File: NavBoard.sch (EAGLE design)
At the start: 11 parts, among them U2 LSM9DS1

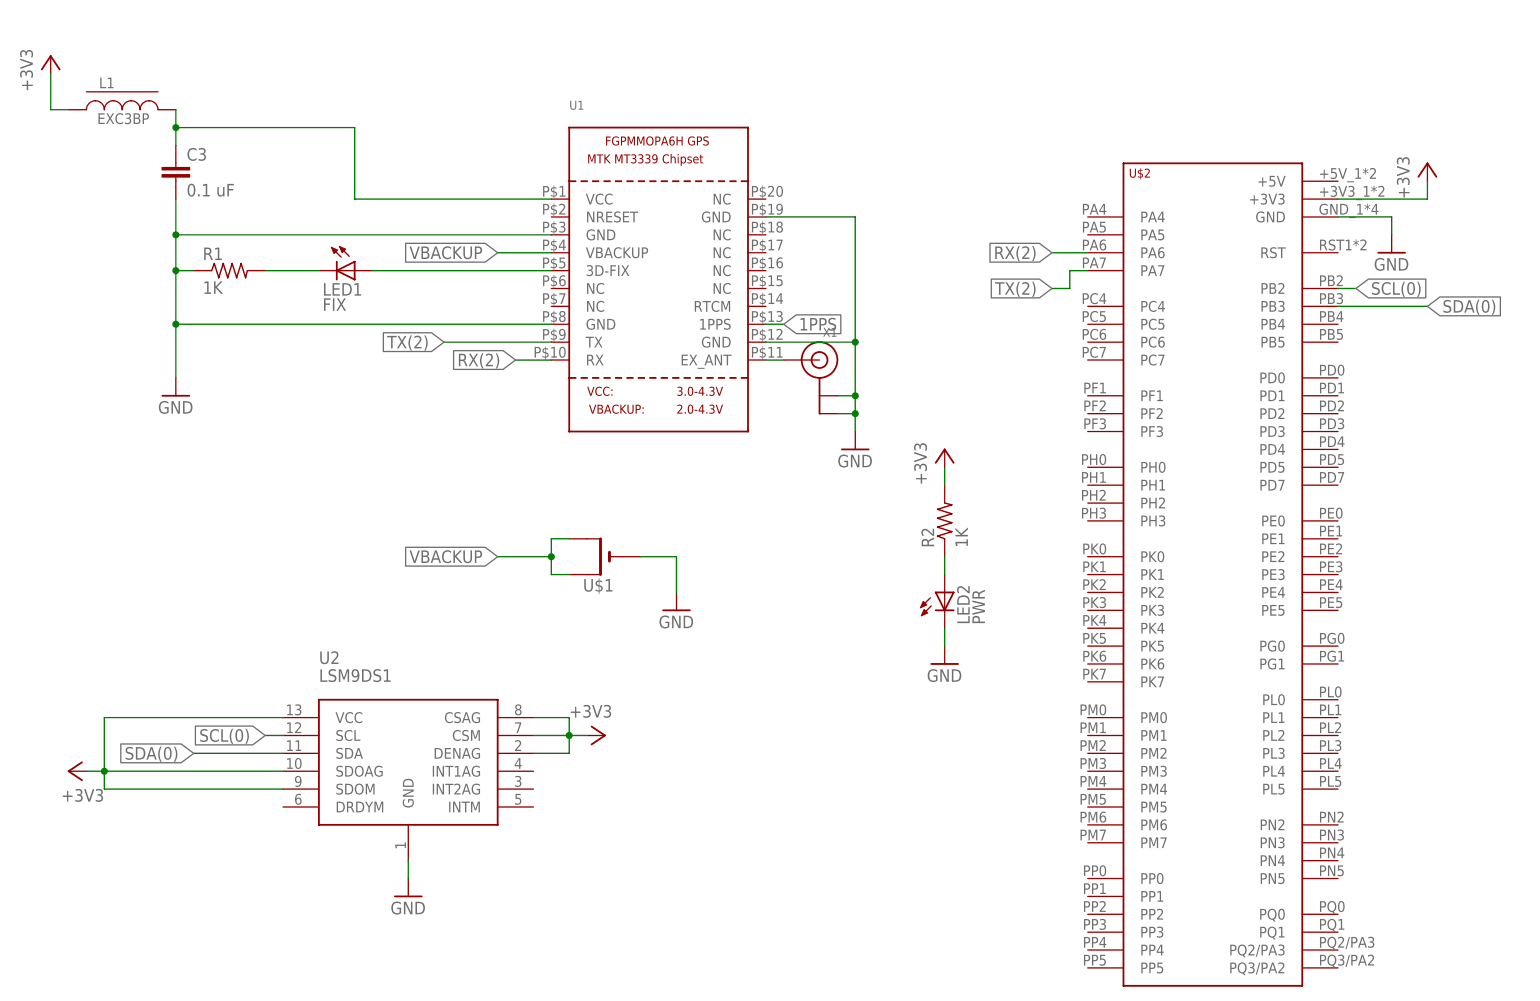
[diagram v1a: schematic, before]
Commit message: Completed first version of PCB design and added power connectors and regulator to schematic and board
Completed first version of board design, added 12v anderson connectors
to schematic along with 5v regulator and 10 uF capacitors, and changed
RX(2) and TX(2) to RX(6) and TX(6).
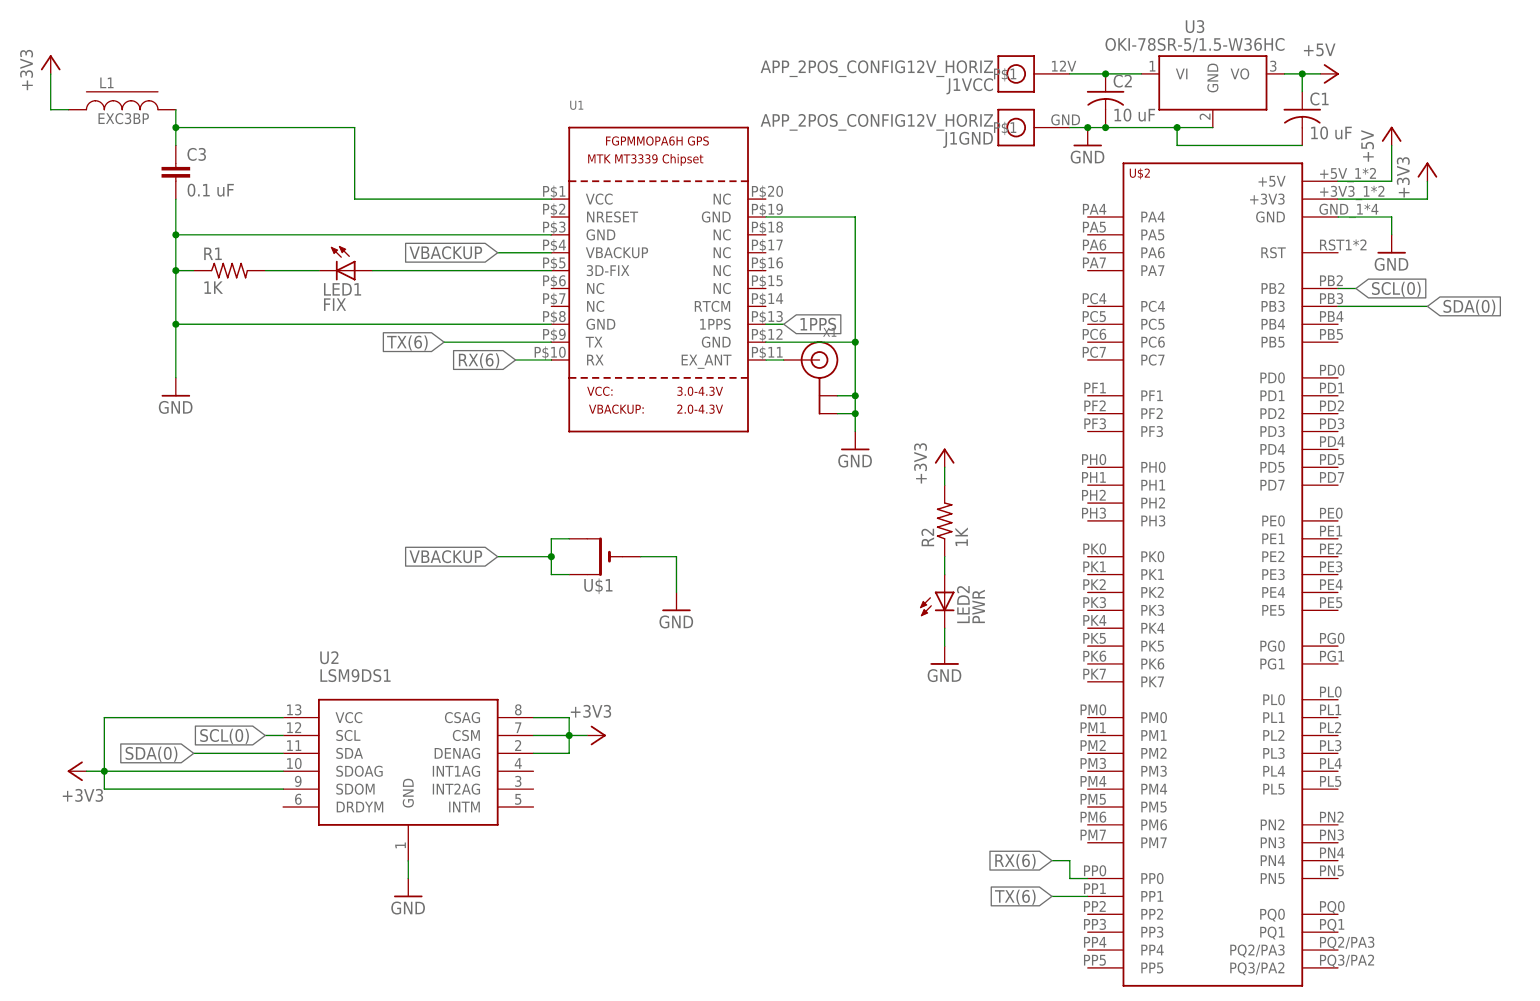
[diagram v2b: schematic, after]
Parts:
- added C1, C2: 10 uF, resistor:C-USC0603
- added J1: APP_2POS_CONFIG12V_HORIZ, MRDT-Connectors:APP_2POS_CONFIG12V_HORIZ
- added U3: OKI-78SR-5/1.5-W36HC, MRDT-ICs:OKI-78SR-5/1.5-W36HC
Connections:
- removed net RX(2): U$2.PA6, U1.RX
- removed net TX(2): U$2.PA7, U1.TX
- new net +5V: C1.1, U$2.+5V, U3.VO
- new net N$1: C2.1, J1VCC.P$1, U3.VI
- new net RX(6): U$2.PP0, U1.RX
- new net TX(6): U$2.PP1, U1.TX
- net GND: now also C1.2, C2.2, J1GND.P$1, U3.GND
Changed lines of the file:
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@@
 <layer number="128" name="_bValues" color="7" fill="1" visible="no" active="yes"/>
 <layer number="129" name="Mask" color="7" fill="1" visible="yes" active="yes"/>
+<layer number="130" name="130bmp" color="7" fill="1" visible="yes" active="yes"/>
 <layer number="131" name="tAdjust" color="7" fill="1" visible="no" active="yes"/>
 <layer number="132" name="bAdjust" color="7" fill="1" visible="no" active="yes"/>
@@
 <layer number="143" name="PMD" color="7" fill="1" visible="no" active="yes"/>
 <layer number="144" name="Drill_legend" color="7" fill="1" visible="no" active="yes"/>
+<layer number="145" name="DrillLegend_01-16" color="7" fill="1" visible="yes" active="yes"/>
 <layer number="150" name="Notes" color="7" fill="1" visible="no" active="yes"/>
 <layer number="151" name="HeatSink" color="7" fill="1" visible="no" active="yes"/>
@@
 <part name="+3V5" library="supply1" deviceset="+3V3" device=""/>
 <part name="GND3" library="supply1" deviceset="GND" device=""/>
+<part name="J1" library="MRDT-Connectors" deviceset="APP_2POS_CONFIG" device="12V_HORIZ"/>
+<part name="U3" library="MRDT-ICs" deviceset="OKI-78SR-*/1.5-W36?C" device="H" technology="5"/>
+<part name="GND4" library="supply1" deviceset="GND" device=""/>
+<part name="P+1" library="supply1" deviceset="+5V" device=""/>
+<part name="P+2" library="supply1" deviceset="+5V" device=""/>
+<part name="C1" library="resistor" deviceset="C-US" device="C0603" value="10 uF"/>
+<part name="C2" library="resistor" deviceset="C-US" device="C0603" value="10 uF"/>
 </parts>
 <sheets>
@@
 <instance part="+3V5" gate="G$1" x="55.88" y="-15.24" rot="R270"/>
 <instance part="GND3" gate="1" x="27.94" y="-38.1"/>
+<instance part="J1" gate="GND" x="114.3" y="71.12" rot="R180"/>
+<instance part="J1" gate="VCC" x="114.3" y="78.74" rot="R180"/>
+<instance part="U3" gate="G$1" x="139.7" y="78.74"/>
+<instance part="GND4" gate="1" x="124.46" y="68.58"/>
+<instance part="P+1" gate="1" x="160.02" y="78.74" rot="R270"/>
+<instance part="P+2" gate="1" x="167.64" y="71.12"/>
+<instance part="C1" gate="G$1" x="154.94" y="73.66"/>
+<instance part="C2" gate="G$1" x="127" y="76.2"/>
 </instances>
 <busses>
@@
 <wire x1="27.94" y1="-35.56" x2="27.94" y2="-33.02" width="0.1524" layer="91"/>
 </segment>
+<segment>
+<pinref part="J1" gate="GND" pin="P$1"/>
+<pinref part="U3" gate="G$1" pin="GND"/>
+<wire x1="121.92" y1="71.12" x2="124.46" y2="71.12" width="0.1524" layer="91"/>
+<pinref part="GND4" gate="1" pin="GND"/>
+<wire x1="124.46" y1="71.12" x2="127" y2="71.12" width="0.1524" layer="91"/>
+<junction x="124.46" y="71.12"/>
+<pinref part="C2" gate="G$1" pin="2"/>
+<wire x1="127" y1="71.12" x2="137.16" y2="71.12" width="0.1524" layer="91"/>
+<junction x="127" y="71.12"/>
+<pinref part="C1" gate="G$1" pin="2"/>
+<wire x1="137.16" y1="71.12" x2="142.24" y2="71.12" width="0.1524" layer="91"/>
+<wire x1="154.94" y1="68.58" x2="137.16" y2="68.58" width="0.1524" layer="91"/>
+<wire x1="137.16" y1="68.58" x2="137.16" y2="71.12" width="0.1524" layer="91"/>
+<junction x="137.16" y="71.12"/>
+</segment>
 </net>
 <net name="VBACKUP" class="0">
@@
 </segment>
 </net>
-<net name="RX(2)" class="0">
-<segment>
-<pinref part="U$2" gate="G$1" pin="PA6"/>
-<wire x1="124.46" y1="53.34" x2="119.38" y2="53.34" width="0.1524" layer="91"/>
-<label x="119.38" y="53.34" size="1.778" layer="95" rot="R180" xref="yes"/>
-</segment>
+<net name="TX(6)" class="0">
+<segment>
+<pinref part="U1" gate="G$1" pin="TX"/>
+<wire x1="48.26" y1="40.64" x2="33.02" y2="40.64" width="0.1524" layer="91"/>
+<label x="33.02" y="40.64" size="1.778" layer="95" rot="R180" xref="yes"/>
+</segment>
+<segment>
+<label x="119.38" y="-38.1" size="1.778" layer="95" rot="R180" xref="yes"/>
+<pinref part="U$2" gate="G$1" pin="PP1"/>
+<wire x1="119.38" y1="-38.1" x2="124.46" y2="-38.1" width="0.1524" layer="91"/>
+</segment>
+</net>
+<net name="RX(6)" class="0">
 <segment>
 <pinref part="U1" gate="G$1" pin="RX"/>
@@
 <label x="43.18" y="38.1" size="1.778" layer="95" rot="R180" xref="yes"/>
 </segment>
-</net>
-<net name="TX(2)" class="0">
-<segment>
-<pinref part="U$2" gate="G$1" pin="PA7"/>
-<wire x1="124.46" y1="50.8" x2="121.92" y2="50.8" width="0.1524" layer="91"/>
-<wire x1="121.92" y1="50.8" x2="121.92" y2="48.26" width="0.1524" layer="91"/>
-<wire x1="121.92" y1="48.26" x2="119.38" y2="48.26" width="0.1524" layer="91"/>
-<label x="119.38" y="48.26" size="1.778" layer="95" rot="R180" xref="yes"/>
-</segment>
-<segment>
-<pinref part="U1" gate="G$1" pin="TX"/>
-<wire x1="48.26" y1="40.64" x2="33.02" y2="40.64" width="0.1524" layer="91"/>
-<label x="33.02" y="40.64" size="1.778" layer="95" rot="R180" xref="yes"/>
-</segment>
-</net>
+<segment>
+<wire x1="119.38" y1="-33.02" x2="121.92" y2="-33.02" width="0.1524" layer="91"/>
+<label x="119.38" y="-33.02" size="1.778" layer="95" rot="R180" xref="yes"/>
+<pinref part="U$2" gate="G$1" pin="PP0"/>
+<wire x1="124.46" y1="-35.56" x2="121.92" y2="-35.56" width="0.1524" layer="91"/>
+<wire x1="121.92" y1="-35.56" x2="121.92" y2="-33.02" width="0.1524" layer="91"/>
+</segment>
+</net>
+<net name="N$1" class="0">
+<segment>
+<pinref part="J1" gate="VCC" pin="P$1"/>
+<pinref part="U3" gate="G$1" pin="VI"/>
+<wire x1="121.92" y1="78.74" x2="127" y2="78.74" width="0.1524" layer="91"/>
+<pinref part="C2" gate="G$1" pin="1"/>
+<wire x1="127" y1="78.74" x2="132.08" y2="78.74" width="0.1524" layer="91"/>
+<junction x="127" y="78.74"/>
+</segment>
+</net>
+<net name="+5V" class="0">
+<segment>
+<pinref part="U3" gate="G$1" pin="VO"/>
+<pinref part="P+1" gate="1" pin="+5V"/>
+<wire x1="152.4" y1="78.74" x2="154.94" y2="78.74" width="0.1524" layer="91"/>
+<pinref part="C1" gate="G$1" pin="1"/>
+<wire x1="154.94" y1="78.74" x2="157.48" y2="78.74" width="0.1524" layer="91"/>
+<wire x1="154.94" y1="76.2" x2="154.94" y2="78.74" width="0.1524" layer="91"/>
+<junction x="154.94" y="78.74"/>
+</segment>
+<segment>
+<pinref part="U$2" gate="G$1" pin="+5V"/>
+<wire x1="160.02" y1="63.5" x2="167.64" y2="63.5" width="0.1524" layer="91"/>
+<wire x1="167.64" y1="63.5" x2="167.64" y2="68.58" width="0.1524" layer="91"/>
+<pinref part="P+2" gate="1" pin="+5V"/>
+</segment>
+</net>

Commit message: Finished revision 1 of board design
Schematic: Connected INTM, INT1, INT2, and DRDYM from IMU to pins PL0
through PL3 on the Tiva. Added two new capacitors to power input of the
GPS chip. Added a capacitor to the battery power supply.
Board: Added top layer ground plane with ground plane stitching, added
mounting holes for the navigation board, arranged all component names on
board so they would be visible once they were silk screened, and added
text block with school name, team, logo, and board name.
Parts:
- added C4: 0.01uF, resistor:C-USC0805
- added C5: 1uF, resistor:C-USC0805
- added LOGO1: MRDT_LOGO, MRDT-Hardware:MRDT_LOGO
- C1, C2: device resistor:C-USC0603 -> resistor:C-USC1206
- C3: value 0.1 uF -> 1uF; device rcl:C-EUC0805 -> resistor:C-USC0805
- renumbered U$1 to U4
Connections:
- removed net N$23: LED1.C, R1.2
- removed net N$6: LED1.A, U1.3D-FIX
- new net DRDYM: U$2.PL3, U2.DRDYM
- new net INT1: U$2.PL1, U2.INT1AG
- new net INT2: U$2.PL0, U2.INT2AG
- new net INTM: U$2.PL2, U2.INTM
- new net N$2: LED1.A, R1.1
- new net N$3: R1.2, U1.3D-FIX
- net GND: now also C4.2, C5.2, LED1.C; no longer R1.1
- net N$24: now also C4.1
- net RX(6): now also U$2.PP1; no longer U$2.PP0
- net TX(6): now also U$2.PP0; no longer U$2.PP1
- net VBACKUP: now also C5.1
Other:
- moved on the sheet: LED1, R1
